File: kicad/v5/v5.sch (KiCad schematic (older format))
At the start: 44 parts, among them J1 BNC, J1-1 Head1_1, J1-2 Head1_1, J2 BNC, J2-1 Head1_1, J2-2 Head1_1, J2-3 Head1_1, J3 Green, J3-1 Head1_1, J3-2 Head1_1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

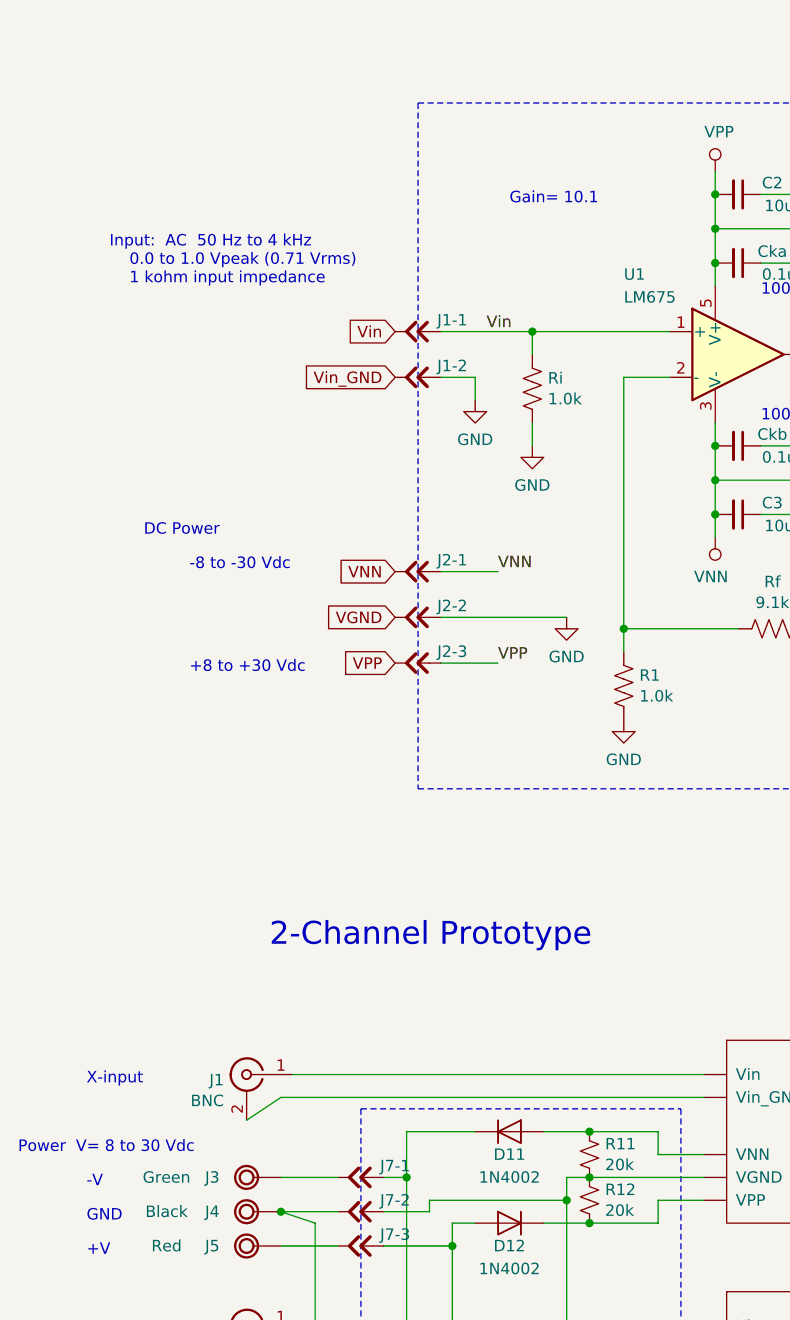
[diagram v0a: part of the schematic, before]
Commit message: Schematic:  Revise input and power notes for operating range.
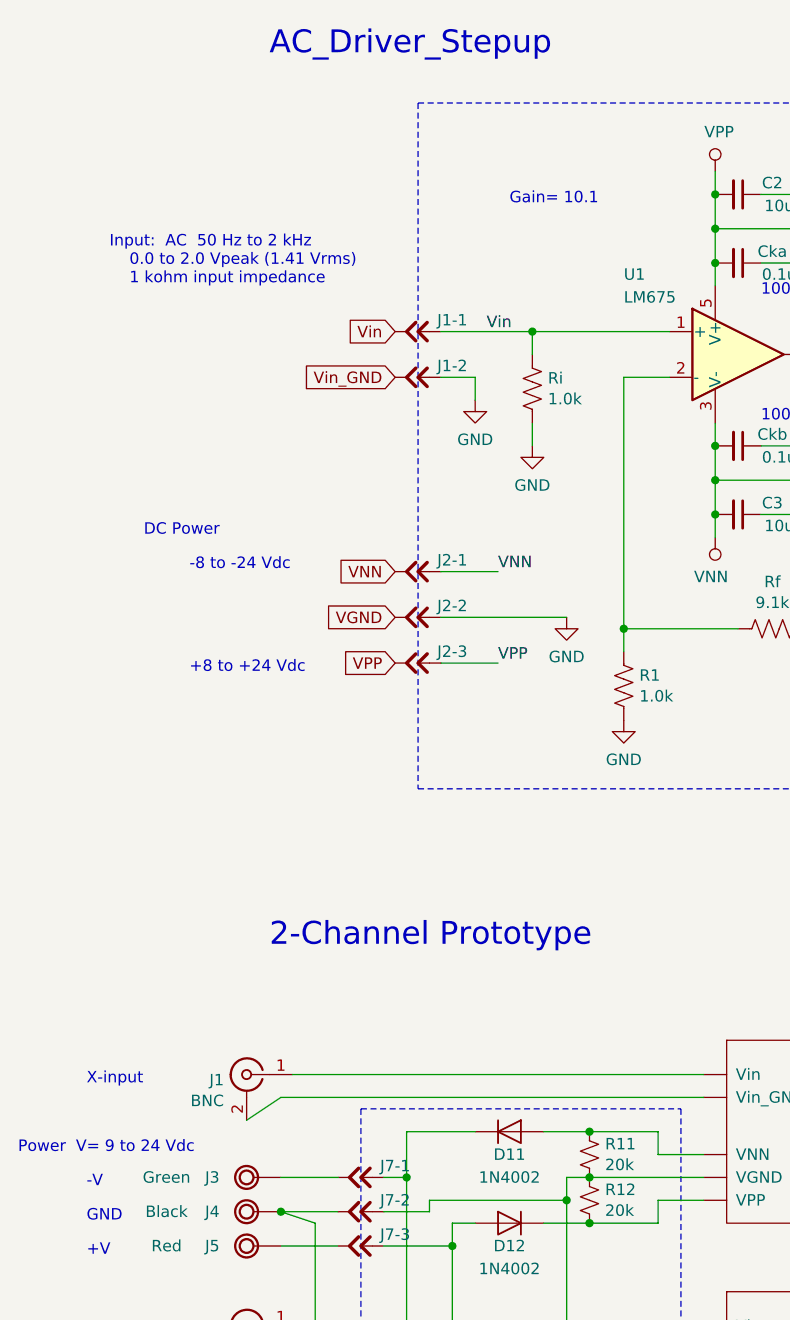
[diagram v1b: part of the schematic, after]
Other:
- note added: "+8 to +24 Vdc"
- note added: "-8 to -24 Vdc"
- note added: "AC_Driver_Stepup"
- note added: "Input: AC 50 Hz to 2 kHz\n 0.0 to 2.0 Vpeak (1.41 Vrms)\n 1 kohm input impedance"
- note added: "Power V= 9 to 24 Vdc"
- note removed: "+8 to +30 Vdc"
- note removed: "-8 to -30 Vdc"
- note removed: "Input: AC 50 Hz to 4 kHz\n 0.0 to 1.0 Vpeak (0.71 Vrms)\n 1 kohm input impedance"
- note removed: "Power V= 8 to 30 Vdc"
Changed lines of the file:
@@
 Sheet 1 1
 Title "Piezo AC Driver - v5, Protoboard"
-Date "2019-04-01"
+Date "2019-04-08"
 Rev ""
 Comp "William A. Hudson"
@@
 VNN
 Text Notes 1300 3600 0    50   ~ 0
-+8 to +30 Vdc
++8 to +24 Vdc
 Text Notes 1300 3150 0    50   ~ 0
--8 to -30 Vdc
+-8 to -24 Vdc
 $Comp
 L _Local:Micro_Con_X_6_panel J6
@@
 2-Channel Prototype
 Text Notes 550  5700 0    50   ~ 0
-Power  V= 8 to 30 Vdc
+Power  V= 9 to 24 Vdc
 Text Notes 5750 5450 0    50   ~ 0
 Yellow
@@
 Gain= 10.1
 Text Notes 950  1900 0    50   ~ 0
-Input:  AC  50 Hz to 4 kHz\n    0.0 to 1.0 Vpeak (0.71 Vrms)\n    1 kohm input impedance
+Input:  AC  50 Hz to 2 kHz\n    0.0 to 2.0 Vpeak (1.41 Vrms)\n    1 kohm input impedance
 Text Notes 5700 3150 0    50   ~ 0
 3W
@@
 Wire Notes Line
 	2050 7500 2050 5500
+Text Notes 1650 900  0    100  ~ 0
+AC_Driver_Stepup
 $EndSCHEMATC
